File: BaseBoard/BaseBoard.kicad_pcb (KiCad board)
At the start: 2 copper layers, 100 x 86 mm, 84 parts, among them J1 PH2.0_1x04, J10 Barrel_Jack_Switch, J11 Conn_01x02_Female, J12 HT396R_1x02, J13 XT30PW, J14 HT396R_1x02, J15 PH2.0_1x03, J2 Raspberry_Pi_2_3, J3 USB_C_Receptacle_USB2.0, J4 PinHeader_2.54_1x04, J5 Conn_01x02_Female, J6 PH2.0_1x03, J7 PH2.0_1x06, J8 PH2.0_1x06, J9 PH2.0_1x06, K1 SRD-12V, Q1 2N7002, SW1 TL3342, SW2 TL3342, U1 BMI088, U2 GD32VF103C8Tx, U3 DRV8870DDA, U4 DRV8870DDA, U5 DRV8870DDA, U5 MINI560, U7 SGM2028-3.3YN5G, U8 BQ34Z100, Y1 8Mhz

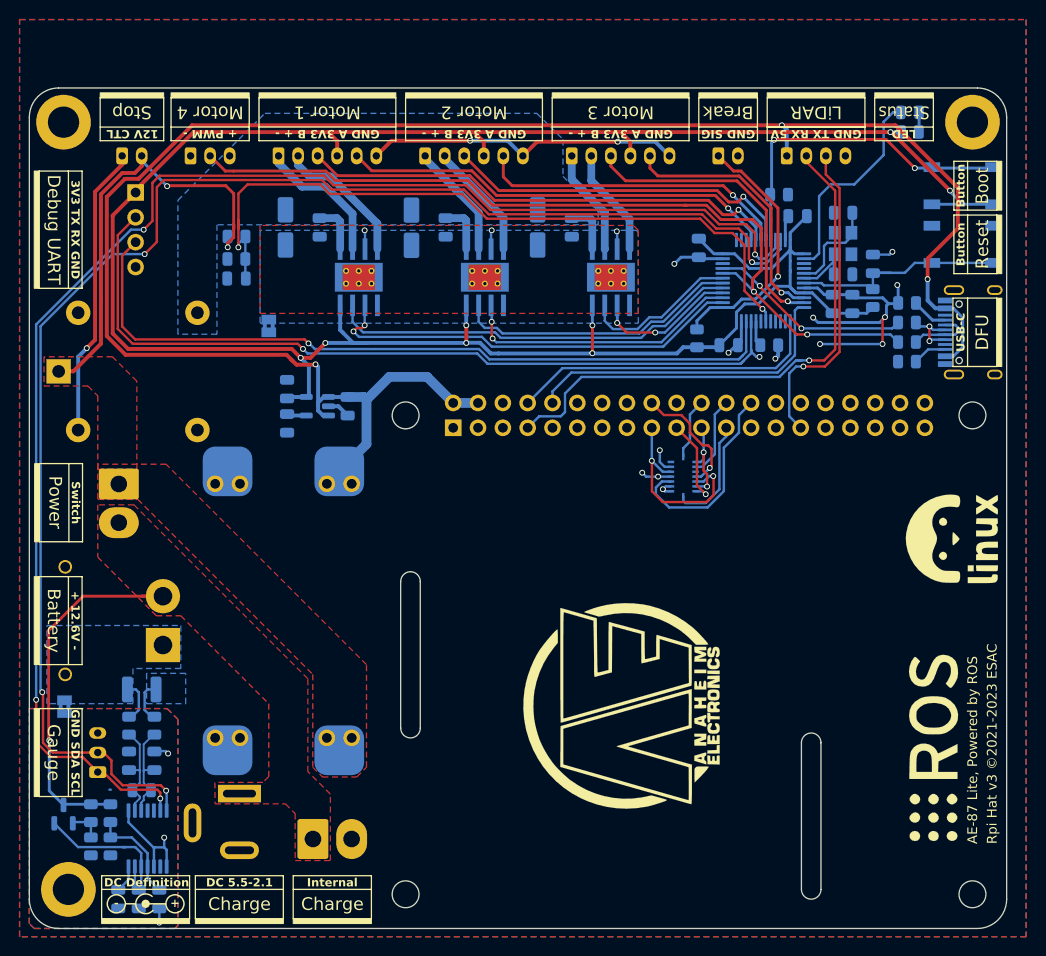
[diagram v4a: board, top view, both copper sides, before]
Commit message: 调整孔位置
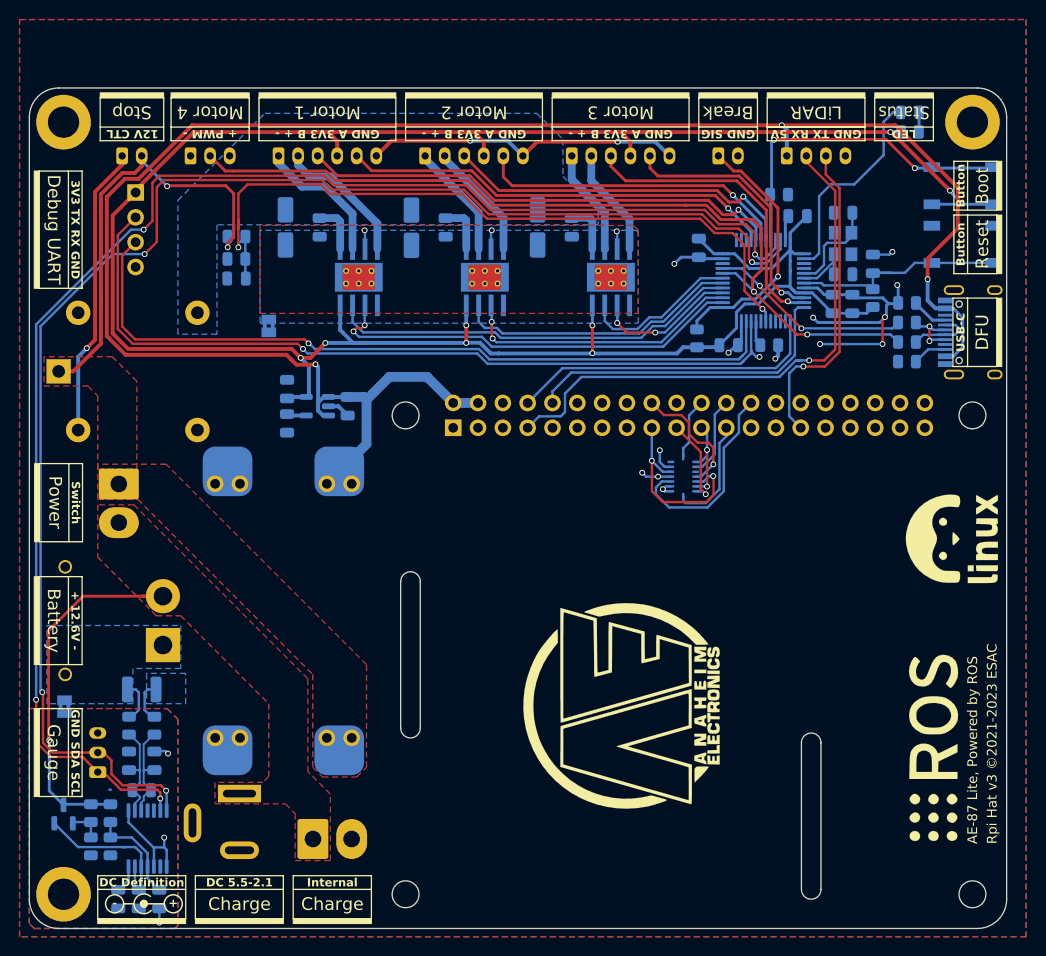
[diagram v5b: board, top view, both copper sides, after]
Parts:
- moved REF** 0.71 mm to (114.0, 145.1)
- moved REF** 0.17 mm to (122.2, 146.0)
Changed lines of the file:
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@@
     )
     (pad_to_mask_clearance 0)
-    (grid_origin 114.49 144.633)
+    (grid_origin 113.99 145.133)
     (pcbplotparams
       (layerselection 0x00010ff_ffffffff)
@@
   )
   (footprint "BaseBoard:MountingHole_3.2mm_M3_DIN965_Pad" locked (layer "F.Cu")
-    (at 114.49 144.633)
+    (at 113.99 145.133)
     (descr "Mounting Hole 3.2mm, M3, DIN965")
     (tags "mounting hole 3.2mm m3 din965")
@@
   )
   (footprint "Symbol:Symbol_Barrel_Polarity" (layer "F.Cu")
-    (at 122.39 146.033)
+    (at 122.215 146.033)
     (descr "Barrel connector polarity indicator")
     (tags "barrel polarity")
@@
     (property "ki_keywords" "R resistor")
     (attr smd)
-    (fp_text reference "R10" (at -2.69 0 180) (layer "B.SilkS")
+    (fp_text reference "R10" (at -3.1 0 180) (layer "B.SilkS")
         (effects (font (size 0.85 0.85) (thickness 0.15)) (justify mirror))
     )
@@
     (property "ki_keywords" "R resistor")
     (attr smd)
-    (fp_text reference "R11" (at 3.0775 0) (layer "B.SilkS")
+    (fp_text reference "R11" (at 3.0875 0) (layer "B.SilkS")
         (effects (font (size 0.85 0.85) (thickness 0.15)) (justify mirror))
     )
@@
   (gr_poly
     (pts
-      (xy 126.89 148.133)
-      (xy 117.89 148.133)
-      (xy 117.89 147.633)
-      (xy 126.89 147.633)
+      (xy 126.49 148.133)
+      (xy 117.49 148.133)
+      (xy 117.49 147.633)
+      (xy 126.49 147.633)
     )
     (stroke (width 0.1) (type solid)) (fill solid) (layer "F.SilkS"))
@@
     )
     (stroke (width 0.1) (type solid)) (fill solid) (layer "F.SilkS"))
-  (gr_line (start 117.89 144.633) (end 126.89 144.633)
+  (gr_line (start 117.49 144.633) (end 126.49 144.633)
     (stroke (width 0.1) (type default)) (layer "F.SilkS"))
   (gr_line (start 206.49 75.133) (end 206.49 70.133)
@@
   (gr_line (start 147.99 66.633) (end 133.99 66.633)
     (stroke (width 0.1) (type default)) (layer "F.SilkS"))
-  (gr_rect (start 117.89 143.233) (end 126.89 147.633)
+  (gr_rect (start 117.49 143.233) (end 126.49 147.633)
     (stroke (width 0.1) (type default)) (fill none) (layer "F.SilkS"))
   (gr_rect (start 148.99 63.633) (end 162.99 68.033)
@@
     (effects (font (size 1.3 1.3) (thickness 0.25)))
   )
-  (gr_text "+" (at 125.39 146.033) (layer "F.SilkS")
+  (gr_text "+" (at 125.215 146.033) (layer "F.SilkS")
     (effects (font (size 0.85 0.85) (thickness 0.15) bold))
   )
@@
     (effects (font (size 1.3 1.3) (thickness 0.25)))
   )
-  (gr_text "-" (at 119.39 146.033) (layer "F.SilkS")
+  (gr_text "-" (at 119.215 146.033) (layer "F.SilkS")
     (effects (font (size 0.85 0.85) (thickness 0.15) bold))
   )
@@
     (effects (font (size 0.85 0.85) (thickness 0.15) bold))
   )
-  (gr_text "DC Definition" (at 122.49 143.933) (layer "F.SilkS")
+  (gr_text "DC Definition" (at 121.99 143.933) (layer "F.SilkS")
     (effects (font (size 0.85 0.85) (thickness 0.15) bold))
   )
@@
   )
   (dimension (type aligned) (layer "Eco1.User")
-    (pts (xy 114.59 145.133) (xy 207.09 145.133))
+    (pts (xy 113.99 145.133) (xy 206.99 145.133))
     (height 18.5)
-    (gr_text "92.5000 mm" (at 160.84 162.483) (layer "Eco1.User")
+    (gr_text "93.0000 mm" (at 160.49 162.483) (layer "Eco1.User")
       (effects (font (size 1 1) (thickness 0.15)))
     )
@@
   )
   (dimension (type aligned) (layer "Eco1.User")
-    (pts (xy 113.99 144.633) (xy 113.99 66.133))
+    (pts (xy 113.99 145.133) (xy 113.99 66.133))
     (height -8)
-    (gr_text "78.5000 mm" (at 104.84 105.383 90) (layer "Eco1.User")
+    (gr_text "79.0000 mm" (at 104.84 105.633 90) (layer "Eco1.User")
       (effects (font (size 1 1) (thickness 0.15)))
     )
@@
   (segment (start 183.844642 89.637673) (end 183.844642 86.512) (width 0.25) (layer "B.Cu") (net 21))
   (segment (start 183.441157 90.041157) (end 183.844642 89.637673) (width 0.25) (layer "B.Cu") (net 21))
-  (segment (start 179.395299 99.2) (end 178.085 97.889701) (width 0.25) (layer "F.Cu") (net 22))
-  (segment (start 178.085 97.889701) (end 178.085 96.985) (width 0.25) (layer "F.Cu") (net 22))
+  (segment (start 180.49 99.444) (end 179.979 98.933) (width 0.25) (layer "F.Cu") (net 22))
+  (segment (start 180.4755 101.144073) (end 180.49 101.129573) (width 0.25) (layer "F.Cu") (net 22))
+  (segment (start 180.49 101.129573) (end 180.49 99.444) (width 0.25) (layer "F.Cu") (net 22))
   (segment (start 177.2 96.1) (end 175.417 96.1) (width 0.25) (layer "F.Cu") (net 22))
-  (segment (start 179.935 99.2) (end 179.395299 99.2) (width 0.25) (layer "F.Cu") (net 22))
-  (segment (start 178.085 96.985) (end 177.2 96.1) (width 0.25) (layer "F.Cu") (net 22))
-  (segment (start 180.109787 101.509787) (end 180.3 101.319574) (width 0.25) (layer "F.Cu") (net 22))
-  (segment (start 180.3 101.319574) (end 180.3 99.565) (width 0.25) (layer "F.Cu") (net 22))
-  (segment (start 180.3 99.565) (end 179.935 99.2) (width 0.25) (layer "F.Cu") (net 22))
+  (segment (start 177.99 96.89) (end 177.2 96.1) (width 0.25) (layer "F.Cu") (net 22))
   (segment (start 175.417 96.1) (end 174.18 94.863) (width 0.25) (layer "F.Cu") (net 22))
-  (via (at 180.109787 101.509787) (size 0.6) (drill 0.4) (layers "F.Cu" "B.Cu") (net 22))
-  (segment (start 179.219574 102.4) (end 180.109787 101.509787) (width 0.25) (layer "B.Cu") (net 22))
-  (segment (start 178.6625 102.4) (end 179.219574 102.4) (width 0.25) (layer "B.Cu") (net 22))
-  (segment (start 178.8 99.483) (end 176.72 97.403) (width 0.25) (layer "F.Cu") (net 23))
-  (segment (start 178.8 103.3) (end 178.8 99.483) (width 0.25) (layer "F.Cu") (net 23))
-  (segment (start 179.7 104.2) (end 178.8 103.3) (width 0.25) (layer "F.Cu") (net 23))
+  (segment (start 178.886396 98.933) (end 177.99 98.036604) (width 0.25) (layer "F.Cu") (net 22))
+  (segment (start 179.979 98.933) (end 178.886396 98.933) (width 0.25) (layer "F.Cu") (net 22))
+  (segment (start 177.99 98.036604) (end 177.99 96.89) (width 0.25) (layer "F.Cu") (net 22))
+  (via (at 180.4755 101.144073) (size 0.6) (drill 0.4) (layers "F.Cu" "B.Cu") (net 22))
+  (segment (start 179.219573 102.4) (end 178.6625 102.4) (width 0.25) (layer "B.Cu") (net 22))
+  (segment (start 180.4755 101.144073) (end 179.219573 102.4) (width 0.25) (layer "B.Cu") (net 22))
+  (segment (start 179.7 104.2) (end 179.19 103.69) (width 0.25) (layer "F.Cu") (net 23))
+  (segment (start 179.19 99.873) (end 176.72 97.403) (width 0.25) (layer "F.Cu") (net 23))
+  (segment (start 179.19 103.69) (end 179.19 99.873) (width 0.25) (layer "F.Cu") (net 23))
   (via (at 179.7 104.2) (size 0.6) (drill 0.4) (layers "F.Cu" "B.Cu") (net 23))
   (segment (start 179.4 103.9) (end 178.6625 103.9) (width 0.25) (layer "B.Cu") (net 23))
@@
   (segment (start 201.5275 65.133) (end 201.5275 67.108) (width 0.3) (layer "B.Cu") (net 48))
   (segment (start 201.5275 67.108) (end 201.5025 67.133) (width 0.3) (layer "B.Cu") (net 48))
-  (segment (start 179.484787 101.784787) (end 179.484787 99.915213) (width 0.25) (layer "F.Cu") (net 49))
-  (segment (start 179.83686 102.13686) (end 179.484787 101.784787) (width 0.25) (layer "F.Cu") (net 49))
-  (segment (start 179.83686 103.4123) (end 179.83686 102.13686) (width 0.25) (layer "F.Cu") (net 49))
-  (via (at 179.484787 99.915213) (size 0.6) (drill 0.4) (layers "F.Cu" "B.Cu") (net 49))
+  (segment (start 179.830661 99.667839) (end 179.83686 99.674038) (width 0.25) (layer "F.Cu") (net 49))
+  (segment (start 179.83686 99.674038) (end 179.83686 103.4123) (width 0.25) (layer "F.Cu") (net 49))
+  (via (at 179.830661 99.667839) (size 0.6) (drill 0.4) (layers "F.Cu" "B.Cu") (net 49))
   (via (at 179.83686 103.4123) (size 0.6) (drill 0.4) (layers "F.Cu" "B.Cu") (net 49))
-  (segment (start 179.2 100.9) (end 178.6625 100.9) (width 0.25) (layer "B.Cu") (net 49))
-  (segment (start 179.484787 97.627787) (end 179.26 97.403) (width 0.25) (layer "B.Cu") (net 49))
+  (segment (start 179.830661 100.269339) (end 179.2 100.9) (width 0.25) (layer "B.Cu") (net 49))
   (segment (start 179.83686 103.4123) (end 179.628416 103.4123) (width 0.25) (layer "B.Cu") (net 49))
-  (segment (start 179.484787 99.915213) (end 179.484787 97.627787) (width 0.25) (layer "B.Cu") (net 49))
-  (segment (start 179.484787 100.615213) (end 179.2 100.9) (width 0.25) (layer "B.Cu") (net 49))
   (segment (start 179.616116 103.4) (end 178.6625 103.4) (width 0.25) (layer "B.Cu") (net 49))
-  (segment (start 179.484787 99.915213) (end 179.484787 100.615213) (width 0.25) (layer "B.Cu") (net 49))
   (segment (start 179.628416 103.4123) (end 179.616116 103.4) (width 0.25) (layer "B.Cu") (net 49))
-  (segment (start 177.4 99.5) (end 178.085 98.815) (width 0.25) (layer "B.Cu") (net 52))
-  (segment (start 178.085 96.038) (end 179.26 94.863) (width 0.25) (layer "B.Cu") (net 52))
-  (segment (start 178.085 98.815) (end 178.085 96.038) (width 0.25) (layer "B.Cu") (net 52))
+  (segment (start 179.2 100.9) (end 178.6625 100.9) (width 0.25) (layer "B.Cu") (net 49))
+  (segment (start 179.830661 97.973661) (end 179.26 97.403) (width 0.25) (layer "B.Cu") (net 49))
+  (segment (start 179.830661 99.667839) (end 179.830661 100.269339) (width 0.25) (layer "B.Cu") (net 49))
+  (segment (start 179.830661 99.667839) (end 179.830661 97.973661) (width 0.25) (layer "B.Cu") (net 49))
   (segment (start 177.4 100.3875) (end 177.4 99.5) (width 0.25) (layer "B.Cu") (net 52))
+  (segment (start 177.4 99.5) (end 177.99 98.91) (width 0.25) (layer "B.Cu") (net 52))
+  (segment (start 177.99 96.133) (end 179.26 94.863) (width 0.25) (layer "B.Cu") (net 52))
+  (segment (start 177.99 98.91) (end 177.99 96.133) (width 0.25) (layer "B.Cu") (net 52))
   (segment (start 177.6 105.1) (end 179.7 105.1) (width 0.25) (layer "B.Cu") (net 53))
   (segment (start 181.8 98.275) (end 181.8 97.403) (width 0.25) (layer "B.Cu") (net 53))

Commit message: 修改部分封装和值
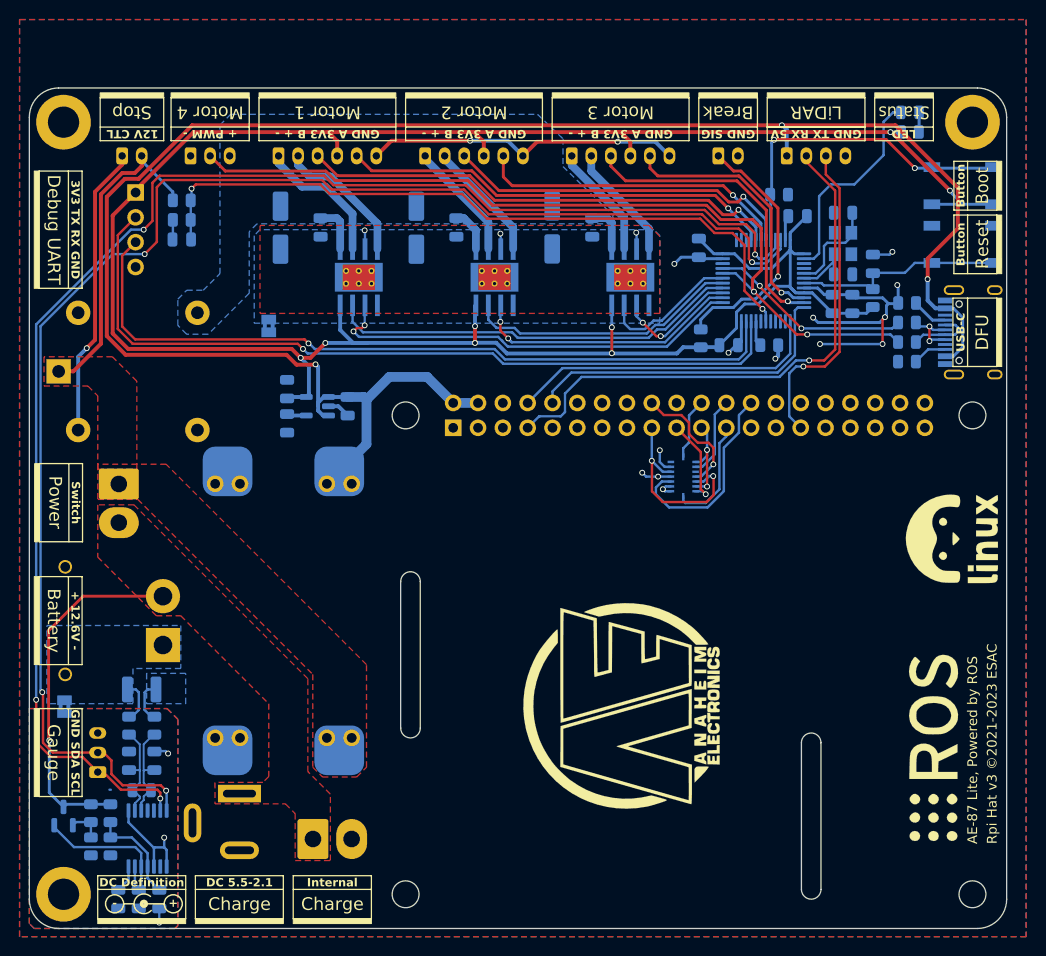
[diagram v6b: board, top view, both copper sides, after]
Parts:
- C1, C2: value 6pF -> 12pF
- C10, C11, C9: footprint Capacitor_SMD:CP_Elec_4x5.4 -> Capacitor_SMD:CP_Elec_5x5.4
- J10: value Barrel_Jack_Switch -> DC5.5/2.1
- J11, J5: value Conn_01x02_Female -> PH2.0_1x02
- R14, R16: value 100 -> 100R
- Y1: value 8Mhz -> 8MHz
- moved C18 6.88 mm to (126.1, 78.1)
- moved R11 6.87 mm to (126.1, 76.1)
- moved R10 6.71 mm to (126.1, 74.1)
- moved C14 2.09 mm to (168.1, 76.9)
- moved U5 1.99 mm to (172.0, 82.0)
- moved C11 1.49 mm to (164.0, 76.9)
- moved C13 1.10 mm to (154.2, 76.9)
- moved U4 0.99 mm to (158.1, 82.0)
- moved C10 0.51 mm to (136.2, 76.9)
- moved C9 0.50 mm to (150.1, 76.9)
- moved R9 0.39 mm to (179.2, 88.2)
- moved Q1 0.20 mm to (114.0, 137.1)
- moved C12 0.09 mm to (140.3, 76.9)
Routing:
- net +12V: track 46.7 -> 33.1 mm, vias 2 -> 0
- net /PWM3_ON: track 16.4 -> 12.6 mm
- net /ADC: track 75.7 -> 73.3 mm
- net +3V3: track 253.2 -> 251.0 mm
- net +BATT: track 38.8 -> 36.7 mm
- net /PWM3: track 16.2 -> 14.3 mm
- net Net-(U2-NRST): track 23.5 -> 21.7 mm
- net /DEBUG_TX: track 83.7 -> 82.2 mm, vias 2 -> 1
- net GND: track 93.4 -> 94.9 mm
- net /OSCOUT: track 7.80 -> 6.63 mm
- net /PWM2: track 29.3 -> 28.2 mm
- net +12VA: track 15.4 -> 14.5 mm
- net /Motor/MOT3_P: track 11.2 -> 12.0 mm
- net /PWM2_ON: track 29.0 -> 28.2 mm
- net /Motor/MOT3_N: track 12.5 -> 11.8 mm
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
